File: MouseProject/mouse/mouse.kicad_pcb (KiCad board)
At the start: 2 copper layers, 58 x 102.5 mm, 66 parts, among them J1 B4B-PH-K-S_LF__SN_, J2 B02B-PASK-1, J3 B4B-PH-K-S_LF__SN_, J4 5051100492, J5 USB_B_Micro, J6 5051100492, Q7 MMBT3904-7-F, Q8 MMBT3904-7-F, Q9 MMBT3904-7-F, U1 AP2112K-3.3, U2 MIC5219-5.0YM5-TR, U3 TPS78319DDCT

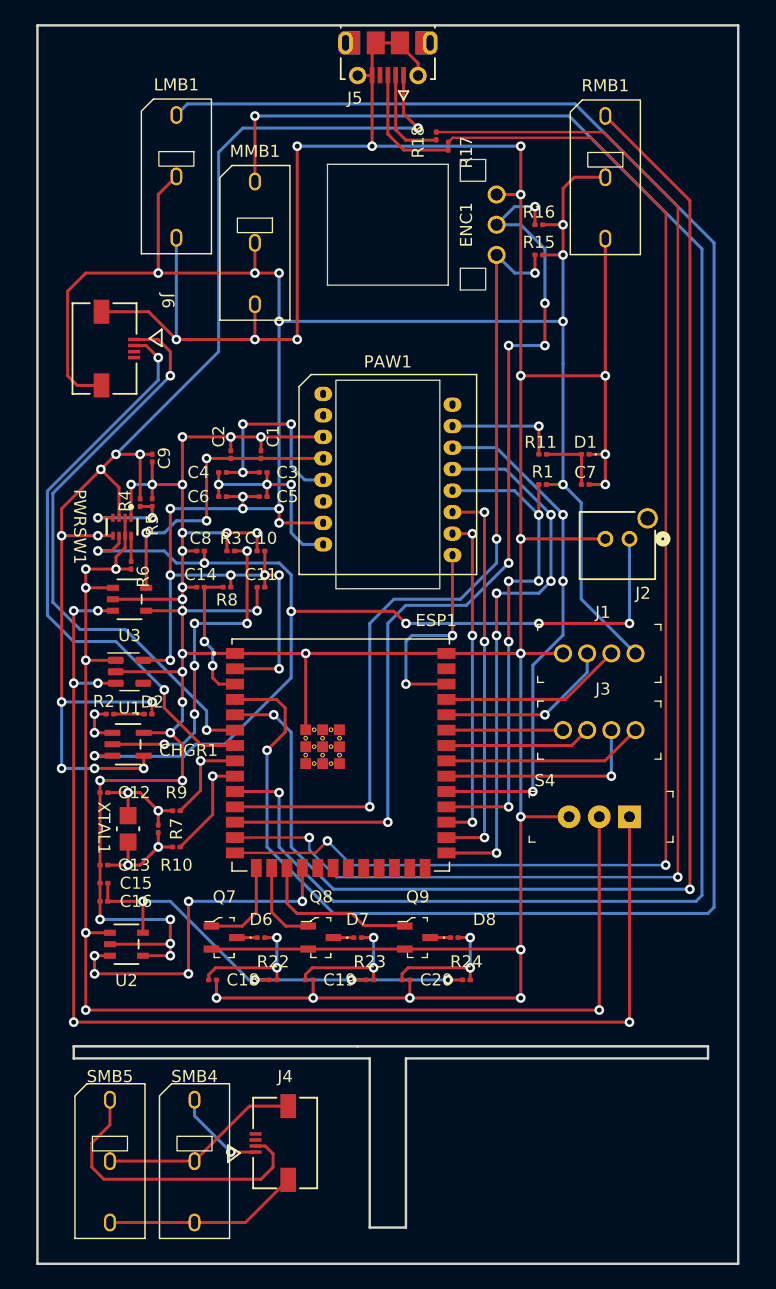
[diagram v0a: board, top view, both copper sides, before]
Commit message: Update for dev board
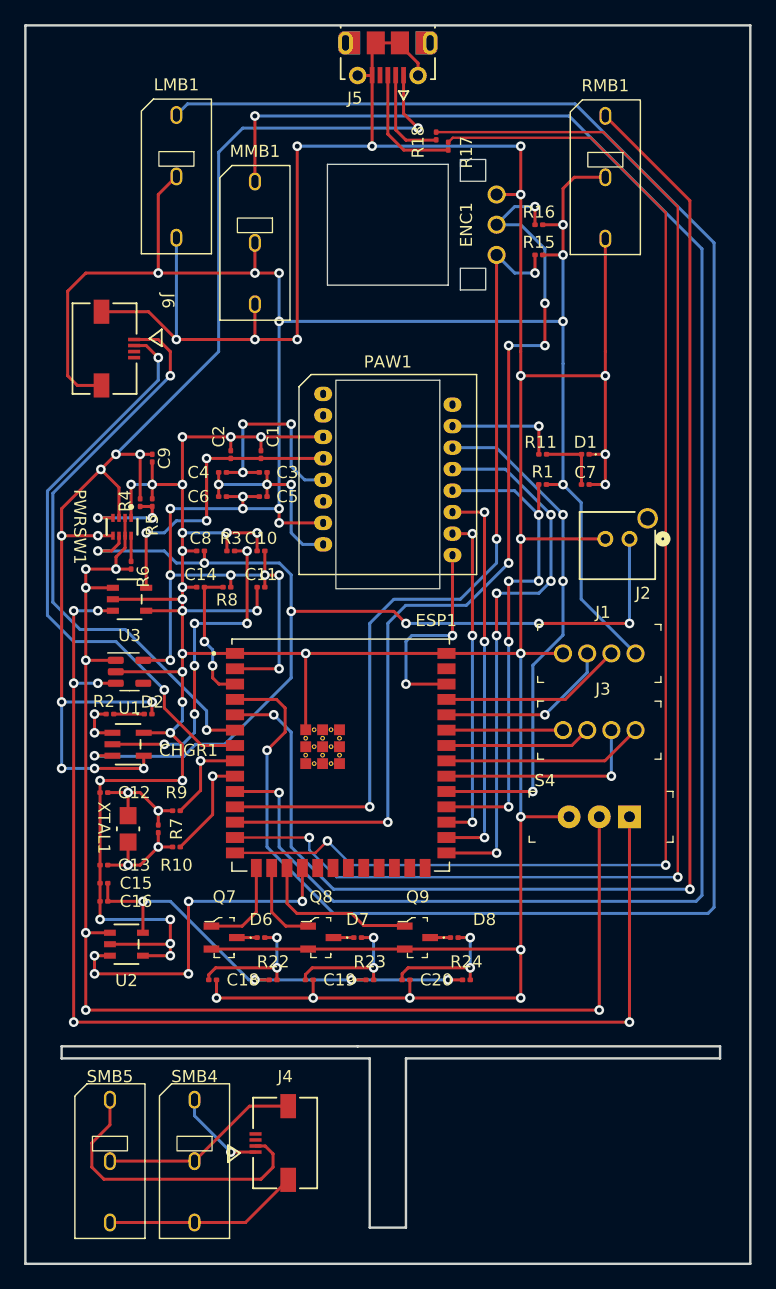
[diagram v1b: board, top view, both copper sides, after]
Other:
- board size 58 x 102.5 mm -> 60 x 102.5 mm
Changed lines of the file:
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@@
     )
   )
-  (gr_rect (start 47.2 20.45) (end 105.2 122.95)
+  (gr_rect (start 46.2 20.45) (end 106.2 122.95)
     (stroke (width 0.2) (type default)) (fill none) (layer "Edge.Cuts"))
   (gr_rect (start 71.2 31.95) (end 81.2 41.95)
@@
   (gr_poly
     (pts
-      (xy 50.2 105.95)
+      (xy 49.2 105.95)
       (xy 74.7 105.95)
       (xy 74.7 119.95)
       (xy 77.7 119.95)
       (xy 77.7 105.95)
-      (xy 102.7 105.95)
-      (xy 102.7 104.95)
+      (xy 103.7 105.95)
+      (xy 103.7 104.95)
       (xy 73.7 104.95)
-      (xy 50.2 104.95)
+      (xy 49.2 104.95)
     )
     (stroke (width 0.2) (type solid)) (fill none) (layer "Edge.Cuts"))

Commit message: Update for final board rev1
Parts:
- removed C15: 22uF, Capacitor_SMD:C_0201_0603Metric
- removed C16: 0.1uF, Capacitor_SMD:C_0201_0603Metric
- removed C18, C19, C20: 4.7uF, Capacitor_SMD:C_0201_0603Metric
- removed D6: LED_R, LED_SMD:LED_0201_0603Metric
- removed D7: LED_G, LED_SMD:LED_0201_0603Metric
- removed D8: LED_B, LED_SMD:LED_0201_0603Metric
- removed J1, J3: B4B-PH-K-S_LF__SN_, digikey-footprints:PinHeader_1x4_P2mm_Drill1mm
- removed Q7, Q8, Q9: MMBT3904-7-F, digikey-footprints:SOT-23-3
- removed R22, R23, R24: ??, Resistor_SMD:R_0201_0603Metric
- removed U2: MIC5219-5.0YM5-TR, MIC5219_5_0YM5_TR:SOT-23-5_M5_MCH
- added R12: 10k, Resistor_SMD:R_0201_0603Metric, F.Cu at (198.7, 54.0)
- added R13: 10k, Resistor_SMD:R_0201_0603Metric, F.Cu at (198.7, 56.5)
- added R14: 10k, Resistor_SMD:R_0201_0603Metric, F.Cu at (198.7, 51.5)
- added R19: 10k, Resistor_SMD:R_0201_0603Metric, F.Cu at (244.2, 56.6)
- added R20: 10k, Resistor_SMD:R_0201_0603Metric, F.Cu at (244.2, 51.5)
- moved R6 192.2 mm to (246.3, 83.1)
- moved PWRSW1 192.2 mm to (245.6, 79.5)
- moved R5 189.8 mm to (245.8, 76.5)
- moved R4 189.8 mm to (244.8, 76.5)
- moved U1 184.9 mm to (239.7, 79.0), turned to 90 degrees
- moved C9 184.3 mm to (240.2, 73.5), turned to -90 degrees
- moved CHGR1 182.1 mm to (236.7, 74.1)
- moved R2 179.4 mm to (232.5, 73.2), turned to 0 degrees
- moved D2 174.6 mm to (230.9, 73.2), turned to 180 degrees
- moved C8 173.4 mm to (233.7, 76.1), turned to -90 degrees
- moved C11 172.0 mm to (237.2, 80.5), turned to 90 degrees
- moved C10 171.3 mm to (236.2, 80.5), turned to 90 degrees
- moved R3 169.6 mm to (232.5, 74.1)
- moved J4 161.3 mm to (228.7, 123.5)
- moved SMB4 160.6 mm to (220.4, 119.9)
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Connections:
- ESP1 pad 18: PWR_5V_EN -> SW4_COM
- ESP1 pad 19: unconnected-(ESP1-IO11-Pad19) -> SW3_COM
- ESP1 pad 39: unconnected-(ESP1-IO1-Pad39) -> PWR_1.9V_EN
- ESP1 pad 4: SW1_COM -> SW1_NO
- ESP1 pad 5: SW2_COM -> SW1_NC
- ESP1 pad 6: SW3_COM -> SW2_NO
- ESP1 pad 7: SW4_COM -> SW2_NC
- J4 pad 1: SW3_COM_OFF -> unconnected-(J4-Pad1)
- J4 pad 2: SW4_COM_OFF -> unconnected-(J4-Pad2)
- J4 pad 3: unconnected-(J4-Pad3) -> SW4_COM_OFF
- J4 pad 4: unconnected-(J4-Pad4) -> SW3_COM_OFF
- J6 pad 1: SW3_COM -> unconnected-(J6-Pad1)
- J6 pad 2: SW4_COM -> unconnected-(J6-Pad2)
- J6 pad 3: unconnected-(J6-Pad3) -> SW3_COM
- J6 pad 4: unconnected-(J6-Pad4) -> SW4_COM
- LMB1 pad 1: SW1_COM -> GND
- LMB1 pad 2: PWR_3.3V -> SW1_NO
- LMB1 pad 3: GND -> SW1_NC
- MMB1 pad 2: PWR_3.3V -> SW5_NO
- RMB1 pad 1: SW2_COM -> GND
- RMB1 pad 2: PWR_3.3V -> SW2_NO
- RMB1 pad 3: GND -> SW2_NC
- U3 pad 3: PWR_EN -> PWR_1.9V_EN
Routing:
- net SW1_COM: track 160.7 -> 0.00 mm, vias 1 -> 0
- net SW2_COM: track 116.1 -> 0.00 mm, vias 2 -> 0
- net SCROLL_CLICK: track 145.7 -> 46.8 mm, vias 2 -> 1
- net PWR_EN: track 103.7 -> 5.26 mm, vias 6 -> 0
- net GND: track 408.8 -> 316.8 mm, vias 44 -> 22
- net PWR_1.9V_EN: track 0.00 -> 65.0 mm, vias 0 -> 2
- net SW2_NO: track 0.00 -> 58.7 mm, vias 0 -> 4
- net SW2_NC: track 0.00 -> 54.4 mm, vias 0 -> 4
- net +BATT: track 87.1 -> 35.8 mm, vias 7 -> 2
- net PWR_OUT: track 110.0 -> 70.1 mm, vias 7 -> 2
- net MOTION: track 17.6 -> 56.3 mm, vias 2 -> 4
- net PWR_5V: track 38.5 -> 0.00 mm, vias 4 -> 0
- net SW1_NO: track 0.00 -> 36.7 mm, vias 0 -> 1
- net USB_D-: track 116.7 -> 85.3 mm
- net SW1_NC: track 0.00 -> 30.6 mm, vias 0 -> 1
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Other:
- board size 60 x 102.5 mm -> 59.5 x 101 mm
